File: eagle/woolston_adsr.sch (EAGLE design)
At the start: 39 parts, among them IC1 TL074P, Q1 2N3906, T1 2N3904

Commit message: almost layout
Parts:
- D2, D3: value 1N4148DO35-10 -> 1N4148DO35-7; device diode:1N4148DO35-10 -> diode:1N4148DO35-7
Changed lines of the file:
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@@
 <grid distance="0.1" unitdist="inch" unit="inch" style="lines" multiple="1" display="no" altdistance="0.01" altunitdist="inch" altunit="inch"/>
 <layers>
-<layer number="1" name="Top" color="4" fill="1" visible="no" active="no"/>
-<layer number="16" name="Bottom" color="1" fill="1" visible="no" active="no"/>
-<layer number="17" name="Pads" color="2" fill="1" visible="no" active="no"/>
-<layer number="18" name="Vias" color="2" fill="1" visible="no" active="no"/>
-<layer number="19" name="Unrouted" color="6" fill="1" visible="no" active="no"/>
-<layer number="20" name="Dimension" color="15" fill="1" visible="no" active="no"/>
-<layer number="21" name="tPlace" color="7" fill="1" visible="no" active="no"/>
-<layer number="22" name="bPlace" color="7" fill="1" visible="no" active="no"/>
-<layer number="23" name="tOrigins" color="15" fill="1" visible="no" active="no"/>
-<layer number="24" name="bOrigins" color="15" fill="1" visible="no" active="no"/>
-<layer number="25" name="tNames" color="7" fill="1" visible="no" active="no"/>
-<layer number="26" name="bNames" color="7" fill="1" visible="no" active="no"/>
-<layer number="27" name="tValues" color="7" fill="1" visible="no" active="no"/>
-<layer number="28" name="bValues" color="7" fill="1" visible="no" active="no"/>
+<layer number="1" name="Top" color="4" fill="1" visible="yes" active="no"/>
+<layer number="16" name="Bottom" color="1" fill="1" visible="yes" active="no"/>
+<layer number="17" name="Pads" color="2" fill="1" visible="yes" active="no"/>
+<layer number="18" name="Vias" color="2" fill="1" visible="yes" active="no"/>
+<layer number="19" name="Unrouted" color="6" fill="1" visible="yes" active="no"/>
+<layer number="20" name="Dimension" color="15" fill="1" visible="yes" active="no"/>
+<layer number="21" name="tPlace" color="7" fill="1" visible="yes" active="no"/>
+<layer number="22" name="bPlace" color="7" fill="1" visible="yes" active="no"/>
+<layer number="23" name="tOrigins" color="15" fill="1" visible="yes" active="no"/>
+<layer number="24" name="bOrigins" color="15" fill="1" visible="yes" active="no"/>
+<layer number="25" name="tNames" color="7" fill="1" visible="yes" active="no"/>
+<layer number="26" name="bNames" color="7" fill="1" visible="yes" active="no"/>
+<layer number="27" name="tValues" color="7" fill="1" visible="yes" active="no"/>
+<layer number="28" name="bValues" color="7" fill="1" visible="yes" active="no"/>
 <layer number="29" name="tStop" color="7" fill="3" visible="no" active="no"/>
 <layer number="30" name="bStop" color="7" fill="6" visible="no" active="no"/>
@@
 <layer number="35" name="tGlue" color="7" fill="4" visible="no" active="no"/>
 <layer number="36" name="bGlue" color="7" fill="5" visible="no" active="no"/>
-<layer number="37" name="tTest" color="7" fill="1" visible="no" active="no"/>
-<layer number="38" name="bTest" color="7" fill="1" visible="no" active="no"/>
+<layer number="37" name="tTest" color="7" fill="1" visible="yes" active="no"/>
+<layer number="38" name="bTest" color="7" fill="1" visible="yes" active="no"/>
 <layer number="39" name="tKeepout" color="4" fill="11" visible="no" active="no"/>
 <layer number="40" name="bKeepout" color="1" fill="11" visible="no" active="no"/>
@@
 <layer number="44" name="Drills" color="7" fill="1" visible="no" active="no"/>
 <layer number="45" name="Holes" color="7" fill="1" visible="no" active="no"/>
-<layer number="46" name="Milling" color="3" fill="1" visible="no" active="no"/>
-<layer number="47" name="Measures" color="7" fill="1" visible="no" active="no"/>
-<layer number="48" name="Document" color="7" fill="1" visible="no" active="no"/>
-<layer number="49" name="Reference" color="7" fill="1" visible="no" active="no"/>
-<layer number="50" name="dxf" color="7" fill="1" visible="no" active="no"/>
-<layer number="51" name="tDocu" color="7" fill="1" visible="no" active="no"/>
-<layer number="52" name="bDocu" color="7" fill="1" visible="no" active="no"/>
-<layer number="53" name="tGND_GNDA" color="7" fill="9" visible="no" active="no"/>
-<layer number="54" name="bGND_GNDA" color="1" fill="9" visible="no" active="no"/>
-<layer number="56" name="wert" color="7" fill="1" visible="no" active="no"/>
-<layer number="57" name="tCAD" color="7" fill="1" visible="no" active="no"/>
-<layer number="59" name="tCarbon" color="7" fill="1" visible="no" active="no"/>
-<layer number="60" name="bCarbon" color="7" fill="1" visible="no" active="no"/>
+<layer number="46" name="Milling" color="3" fill="1" visible="yes" active="no"/>
+<layer number="47" name="Measures" color="7" fill="1" visible="yes" active="no"/>
+<layer number="48" name="Document" color="7" fill="1" visible="yes" active="no"/>
+<layer number="49" name="Reference" color="7" fill="1" visible="yes" active="no"/>
+<layer number="50" name="dxf" color="7" fill="1" visible="yes" active="no"/>
+<layer number="51" name="tDocu" color="7" fill="1" visible="yes" active="no"/>
+<layer number="52" name="bDocu" color="7" fill="1" visible="yes" active="no"/>
+<layer number="53" name="tGND_GNDA" color="7" fill="9" visible="yes" active="no"/>
+<layer number="54" name="bGND_GNDA" color="1" fill="9" visible="yes" active="no"/>
+<layer number="56" name="wert" color="7" fill="1" visible="yes" active="no"/>
+<layer number="57" name="tCAD" color="7" fill="1" visible="yes" active="no"/>
+<layer number="59" name="tCarbon" color="7" fill="1" visible="yes" active="no"/>
+<layer number="60" name="bCarbon" color="7" fill="1" visible="yes" active="no"/>
 <layer number="90" name="Modules" color="5" fill="1" visible="yes" active="yes"/>
 <layer number="91" name="Nets" color="2" fill="1" visible="yes" active="yes"/>
@@
 <part name="C7" library="rcl" deviceset="C-US" device="050-024X044" value="10n"/>
 <part name="GND11" library="supply1" deviceset="GND" device=""/>
-<part name="D2" library="diode" deviceset="1N4148" device="DO35-10" value="1N4148DO35-10"/>
+<part name="D2" library="diode" deviceset="1N4148" device="DO35-7" value="1N4148DO35-7"/>
 <part name="REL" library="pot" deviceset="3RP/1610N" device="" value="500k"/>
 <part name="ATT" library="pot" deviceset="3RP/1610N" device="" value="1M log"/>
@@
 <part name="R13" library="rcl" deviceset="R-US_" device="0207/10" value="10k"/>
 <part name="R14" library="rcl" deviceset="R-US_" device="0207/10" value="1k"/>
-<part name="D3" library="diode" deviceset="1N4148" device="DO35-10" value="1N4148DO35-10"/>
+<part name="D3" library="diode" deviceset="1N4148" device="DO35-7" value="1N4148DO35-7"/>
 <part name="R15" library="rcl" deviceset="R-US_" device="0207/10" value="4k7"/>
 <part name="LFO_SW_1" library="solpad" deviceset="LSP11" device=""/>

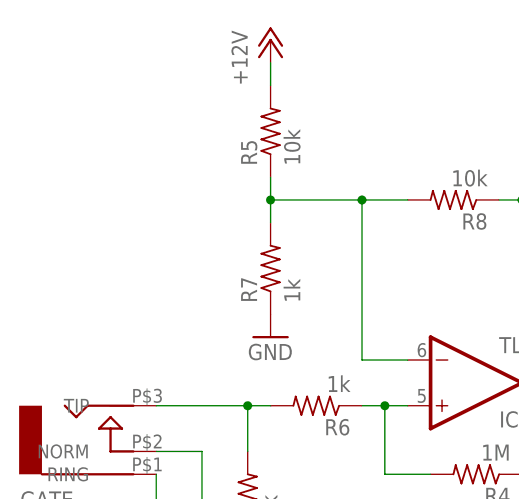
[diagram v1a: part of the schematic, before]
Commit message: fixed power to 074 and twiggled some
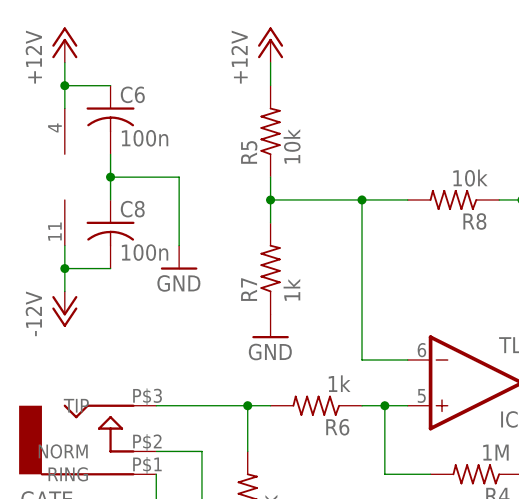
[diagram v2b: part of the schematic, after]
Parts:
- added C6, C8: 100n, rcl:C-US050-024X044
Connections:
- net +12V: now also C6.1, IC1P.V+
- net -12V: now also C8.2, IC1P.V-
- net GND: now also C6.2, C8.1
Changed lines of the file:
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@@
 <?xml version="1.0" encoding="utf-8"?>
 <!DOCTYPE eagle SYSTEM "eagle.dtd">
-<eagle version="7.2.0">
+<eagle version="7.1.0">
 <drawing>
 <settings>
@@
 <grid distance="0.1" unitdist="inch" unit="inch" style="lines" multiple="1" display="no" altdistance="0.01" altunitdist="inch" altunit="inch"/>
 <layers>
-<layer number="1" name="Top" color="4" fill="1" visible="yes" active="no"/>
-<layer number="16" name="Bottom" color="1" fill="1" visible="yes" active="no"/>
-<layer number="17" name="Pads" color="2" fill="1" visible="yes" active="no"/>
-<layer number="18" name="Vias" color="2" fill="1" visible="yes" active="no"/>
-<layer number="19" name="Unrouted" color="6" fill="1" visible="yes" active="no"/>
-<layer number="20" name="Dimension" color="15" fill="1" visible="yes" active="no"/>
-<layer number="21" name="tPlace" color="7" fill="1" visible="yes" active="no"/>
-<layer number="22" name="bPlace" color="7" fill="1" visible="yes" active="no"/>
-<layer number="23" name="tOrigins" color="15" fill="1" visible="yes" active="no"/>
-<layer number="24" name="bOrigins" color="15" fill="1" visible="yes" active="no"/>
-<layer number="25" name="tNames" color="7" fill="1" visible="yes" active="no"/>
-<layer number="26" name="bNames" color="7" fill="1" visible="yes" active="no"/>
-<layer number="27" name="tValues" color="7" fill="1" visible="yes" active="no"/>
-<layer number="28" name="bValues" color="7" fill="1" visible="yes" active="no"/>
+<layer number="1" name="Top" color="4" fill="1" visible="no" active="no"/>
+<layer number="16" name="Bottom" color="1" fill="1" visible="no" active="no"/>
+<layer number="17" name="Pads" color="2" fill="1" visible="no" active="no"/>
+<layer number="18" name="Vias" color="2" fill="1" visible="no" active="no"/>
+<layer number="19" name="Unrouted" color="6" fill="1" visible="no" active="no"/>
+<layer number="20" name="Dimension" color="15" fill="1" visible="no" active="no"/>
+<layer number="21" name="tPlace" color="7" fill="1" visible="no" active="no"/>
+<layer number="22" name="bPlace" color="7" fill="1" visible="no" active="no"/>
+<layer number="23" name="tOrigins" color="15" fill="1" visible="no" active="no"/>
+<layer number="24" name="bOrigins" color="15" fill="1" visible="no" active="no"/>
+<layer number="25" name="tNames" color="7" fill="1" visible="no" active="no"/>
+<layer number="26" name="bNames" color="7" fill="1" visible="no" active="no"/>
+<layer number="27" name="tValues" color="7" fill="1" visible="no" active="no"/>
+<layer number="28" name="bValues" color="7" fill="1" visible="no" active="no"/>
 <layer number="29" name="tStop" color="7" fill="3" visible="no" active="no"/>
 <layer number="30" name="bStop" color="7" fill="6" visible="no" active="no"/>
@@
 <layer number="35" name="tGlue" color="7" fill="4" visible="no" active="no"/>
 <layer number="36" name="bGlue" color="7" fill="5" visible="no" active="no"/>
-<layer number="37" name="tTest" color="7" fill="1" visible="yes" active="no"/>
-<layer number="38" name="bTest" color="7" fill="1" visible="yes" active="no"/>
+<layer number="37" name="tTest" color="7" fill="1" visible="no" active="no"/>
+<layer number="38" name="bTest" color="7" fill="1" visible="no" active="no"/>
 <layer number="39" name="tKeepout" color="4" fill="11" visible="no" active="no"/>
 <layer number="40" name="bKeepout" color="1" fill="11" visible="no" active="no"/>
@@
 <layer number="44" name="Drills" color="7" fill="1" visible="no" active="no"/>
 <layer number="45" name="Holes" color="7" fill="1" visible="no" active="no"/>
-<layer number="46" name="Milling" color="3" fill="1" visible="yes" active="no"/>
-<layer number="47" name="Measures" color="7" fill="1" visible="yes" active="no"/>
-<layer number="48" name="Document" color="7" fill="1" visible="yes" active="no"/>
-<layer number="49" name="Reference" color="7" fill="1" visible="yes" active="no"/>
-<layer number="50" name="dxf" color="7" fill="1" visible="yes" active="no"/>
-<layer number="51" name="tDocu" color="7" fill="1" visible="yes" active="no"/>
-<layer number="52" name="bDocu" color="7" fill="1" visible="yes" active="no"/>
-<layer number="53" name="tGND_GNDA" color="7" fill="9" visible="yes" active="no"/>
-<layer number="54" name="bGND_GNDA" color="1" fill="9" visible="yes" active="no"/>
-<layer number="56" name="wert" color="7" fill="1" visible="yes" active="no"/>
-<layer number="57" name="tCAD" color="7" fill="1" visible="yes" active="no"/>
-<layer number="59" name="tCarbon" color="7" fill="1" visible="yes" active="no"/>
-<layer number="60" name="bCarbon" color="7" fill="1" visible="yes" active="no"/>
+<layer number="46" name="Milling" color="3" fill="1" visible="no" active="no"/>
+<layer number="47" name="Measures" color="7" fill="1" visible="no" active="no"/>
+<layer number="48" name="Document" color="7" fill="1" visible="no" active="no"/>
+<layer number="49" name="Reference" color="7" fill="1" visible="no" active="no"/>
+<layer number="50" name="dxf" color="7" fill="1" visible="no" active="no"/>
+<layer number="51" name="tDocu" color="7" fill="1" visible="no" active="no"/>
+<layer number="52" name="bDocu" color="7" fill="1" visible="no" active="no"/>
+<layer number="53" name="tGND_GNDA" color="7" fill="9" visible="no" active="no"/>
+<layer number="54" name="bGND_GNDA" color="1" fill="9" visible="no" active="no"/>
+<layer number="56" name="wert" color="7" fill="1" visible="no" active="no"/>
+<layer number="57" name="tCAD" color="7" fill="1" visible="no" active="no"/>
+<layer number="59" name="tCarbon" color="7" fill="1" visible="no" active="no"/>
+<layer number="60" name="bCarbon" color="7" fill="1" visible="no" active="no"/>
 <layer number="90" name="Modules" color="5" fill="1" visible="yes" active="yes"/>
 <layer number="91" name="Nets" color="2" fill="1" visible="yes" active="yes"/>
@@
 <part name="C4" library="rcl" deviceset="C-US" device="050-024X044" value="100n"/>
 <part name="C5" library="rcl" deviceset="C-US" device="050-024X044" value="100n"/>
+<part name="P+5" library="supply1" deviceset="+12V" device=""/>
+<part name="P-2" library="supply1" deviceset="-12V" device=""/>
+<part name="C6" library="rcl" deviceset="C-US" device="050-024X044" value="100n"/>
+<part name="C8" library="rcl" deviceset="C-US" device="050-024X044" value="100n"/>
+<part name="GND9" library="supply1" deviceset="GND" device=""/>
 </parts>
 <sheets>
@@
 <instance part="C4" gate="G$1" x="58.42" y="20.32"/>
 <instance part="C5" gate="G$1" x="58.42" y="7.62"/>
+<instance part="IC1" gate="P" x="10.16" y="86.36"/>
+<instance part="P+5" gate="1" x="10.16" y="101.6"/>
+<instance part="P-2" gate="1" x="10.16" y="71.12"/>
+<instance part="C6" gate="G$1" x="15.24" y="93.98"/>
+<instance part="C8" gate="G$1" x="15.24" y="81.28"/>
+<instance part="GND9" gate="1" x="22.86" y="76.2"/>
 </instances>
 <busses>
@@
 <wire x1="160.02" y1="53.34" x2="160.02" y2="55.88" width="0.1524" layer="91"/>
 </segment>
+<segment>
+<pinref part="IC1" gate="P" pin="V+"/>
+<pinref part="P+5" gate="1" pin="+12V"/>
+<wire x1="10.16" y1="99.06" x2="10.16" y2="96.52" width="0.1524" layer="91"/>
+<pinref part="C6" gate="G$1" pin="1"/>
+<wire x1="10.16" y1="96.52" x2="10.16" y2="93.98" width="0.1524" layer="91"/>
+<wire x1="15.24" y1="96.52" x2="10.16" y2="96.52" width="0.1524" layer="91"/>
+<junction x="10.16" y="96.52"/>
+</segment>
 </net>
 <net name="-12V" class="0">
@@
 <wire x1="58.42" y1="2.54" x2="58.42" y2="0" width="0.1524" layer="91"/>
 <wire x1="58.42" y1="0" x2="50.8" y2="0" width="0.1524" layer="91"/>
+</segment>
+<segment>
+<pinref part="IC1" gate="P" pin="V-"/>
+<pinref part="P-2" gate="1" pin="-12V"/>
+<wire x1="10.16" y1="73.66" x2="10.16" y2="76.2" width="0.1524" layer="91"/>
+<pinref part="C8" gate="G$1" pin="2"/>
+<wire x1="10.16" y1="76.2" x2="10.16" y2="78.74" width="0.1524" layer="91"/>
+<wire x1="15.24" y1="76.2" x2="10.16" y2="76.2" width="0.1524" layer="91"/>
+<junction x="10.16" y="76.2"/>
 </segment>
 </net>
@@
 <wire x1="205.74" y1="17.78" x2="205.74" y2="12.7" width="0.1524" layer="91"/>
 </segment>
+<segment>
+<pinref part="GND9" gate="1" pin="GND"/>
+<wire x1="22.86" y1="78.74" x2="22.86" y2="86.36" width="0.1524" layer="91"/>
+<pinref part="C6" gate="G$1" pin="2"/>
+<pinref part="C8" gate="G$1" pin="1"/>
+<wire x1="15.24" y1="83.82" x2="15.24" y2="86.36" width="0.1524" layer="91"/>
+<wire x1="15.24" y1="86.36" x2="15.24" y2="88.9" width="0.1524" layer="91"/>
+<wire x1="22.86" y1="86.36" x2="15.24" y2="86.36" width="0.1524" layer="91"/>
+<junction x="15.24" y="86.36"/>
+</segment>
 </net>
